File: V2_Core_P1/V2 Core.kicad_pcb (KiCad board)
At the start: 4 copper layers, 90 x 110 mm, 340 parts, among them J1 USB_B, J10 Conn_01x02, J11 Conn_01x02, J12 Conn_01x02, J15 Conn_01x02, J16 Conn_01x02, J2 USB_A, J21 Conn_01x02, J22 Conn_01x02, J23 Conn_01x02, J24 Conn_01x03, J25 Conn_01x03, J26 Conn_01x03, J27 Conn_01x03, J28 Conn_01x03, J29 Conn_01x03, J3 Micro_SD_Card_Det, J30 Conn_01x03_Male, J32 Conn_02x05_Odd_Even, J33 Conn_02x05_Odd_Even, J34 Conn_02x05_Odd_Even, J35 Conn_02x05_Odd_Even, J36 Conn_02x05_Odd_Even, J37 Conn_02x05_Odd_Even, J38 Conn_02x05_Odd_Even, J39 Conn_02x05_Odd_Even, J4 RJ45_Hanrun_HR911105A, J40 Conn_02x05_Odd_Even, J41 Conn_ARM_JTAG_SWD_10, J42 Conn_01x02, J43 Conn_01x02, J44 Conn_01x02, J45 Conn_01x02, J5 Conn_02x20_Odd_Even, J6 Conn_01x03, J7 Conn_01x02, J8 Conn_01x02, J9 Conn_01x02, Q1 2N7002, Q2 2N7002, Q23 CJ2301 S1, Q24 CJ2301 S1, Q26 2N7002, Q27 MBT3906DW1, Q28 SQ3493EV, Q29 MBT3906DW1, Q3 2N7002, Q30 SQ3493EV, Q31 MBT3906DW1, Q32 SQ3493EV, Q4 WSD30L40DN, Q5 WSD3066DN33, Q6 2N7002, Q8 WSD3066DN33, SW1 SW_Push, SW2 TS-1185EC-C-D-B, U1 LAN8720A, U10 TPD4E1U06DCKR, U11 TPD4E1U06DCKR, U12 LMV324, U13 TPD4E1U06DCKR, U14 TPD4E1U06DCKR, U15 74LCX07, U16 MT9700, U17 TPD4E1U06DCKR, U18 MT9700, U19 MT9700, U2 STM32H745XIHx, U20 MT9700, U21 TPS5430DDA, U22 MT3410L, U23 AP22814AW5, U24 LMV331, U25 BD4722G, U4 AT25SF081-SSHF-X, U8 TPD4E1U06DCKR, U9 74HCT541, Y1 Crystal_GND24, Y2 Crystal, Y3 Crystal_GND24

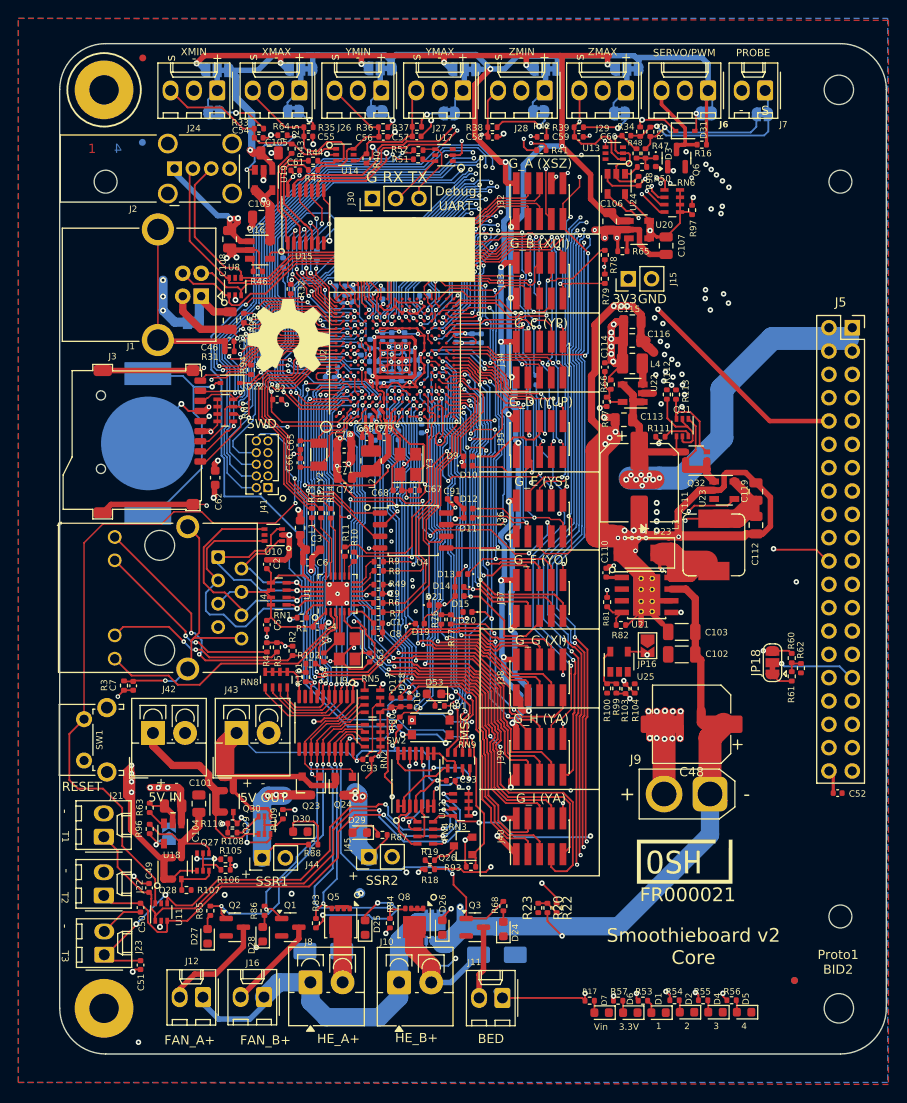
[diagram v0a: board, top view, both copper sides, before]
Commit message: Attach Vmot to UVLO, minor trace cleanup, move C52
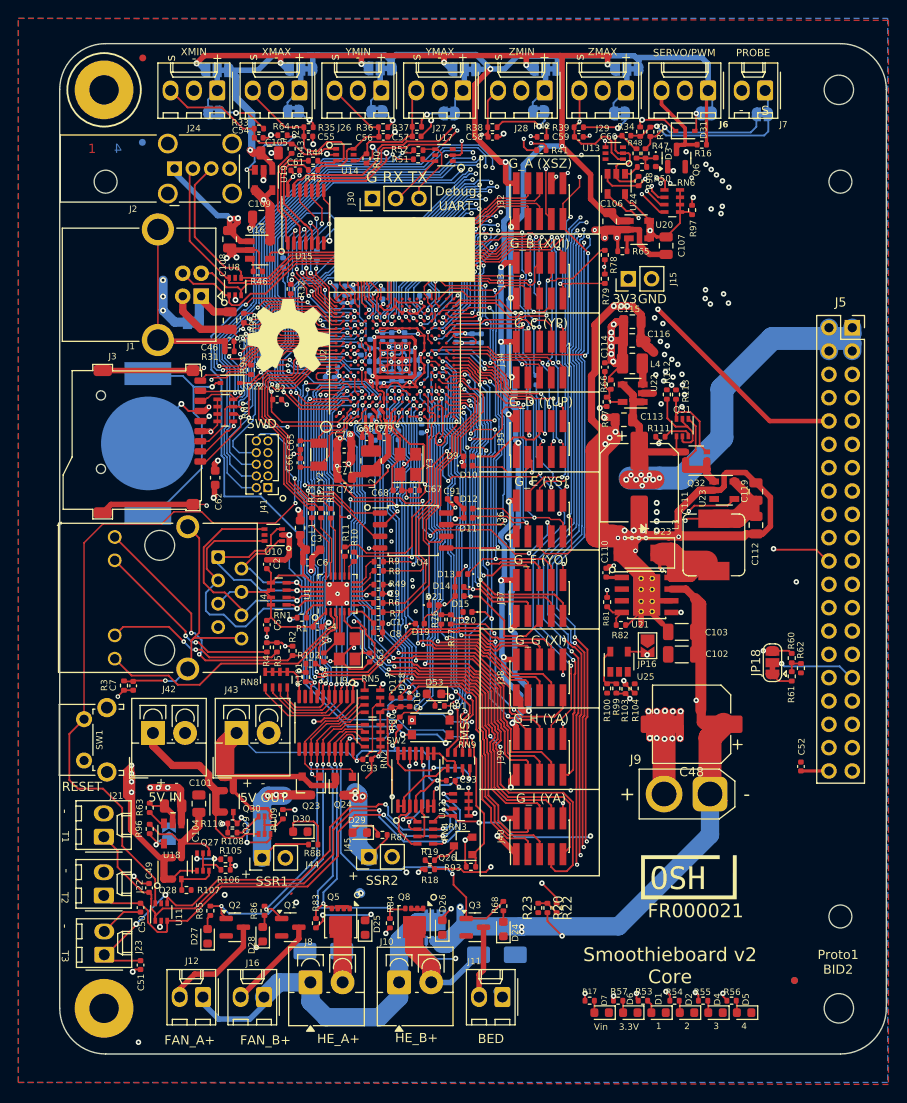
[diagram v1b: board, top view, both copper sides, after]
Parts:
- moved C52 4.94 mm to (180.7, 116.7), turned to 90 degrees
- moved LOGO4 1.76 mm to (168.5, 128.4)
- moved J11 0.10 mm to (148.2, 141.8)
- moved D2 0.05 mm to (168.3, 143.5)
- moved D4 0.05 mm to (171.4, 143.5)
- moved D5 0.05 mm to (174.5, 143.5)
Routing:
- net Net-(D25-A): track 15.3 -> 7.91 mm
- net /5V: track 373.9 -> 379.4 mm
- net VFET: track 117.9 -> 121.1 mm, vias 5 -> 8
- net Net-(Q4-G): track 25.0 -> 24.0 mm
